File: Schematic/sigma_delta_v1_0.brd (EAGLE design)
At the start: 160 x 100 mm, 53 parts, among them IC2 MC78M12CDTG, IC3 UA78M33DCY, J1 SJ1-3523N, Q1 BS170, Q2 BS170, Q3 IRF3707S, Q4 IRF3707S, Q5 BSD223P, X1 1751251, X2 1751248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

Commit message: continued replaceing parts with smd components
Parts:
- removed Q1, Q2: BS170, transistor-small-signal:SOT54E
- added SJ1: (no value), jumper:SJ_2
- added U$4: BSD235N, SamacSys_Parts:SOT65P210X100-6N
- C1: device eagle-ltspice:C3640 -> rcl:C2220K
- C10, C9: device rcl:E2,5-7 -> rcl:UD-10X10_NICHICON
- C2, C3: device rcl:E2-5 -> rcl:UD-6,3X7,7_NICHICON
- moved D2 169.4 mm to (101.6, 31.8), turned to 270 degrees
- moved R8 139.9 mm to (92.7, 36.8), turned to 180 degrees
- moved R14 139.5 mm to (74.9, 44.5), turned to 90 degrees
- moved R13 133.6 mm to (74.9, 49.5), turned to 270 degrees
- moved R7 133.3 mm to (94.0, 57.1), turned to 180 degrees
- moved R15 130.8 mm to (61.0, 44.5), turned to 270 degrees
- moved D3 122.5 mm to (101.6, 52.1), turned to 270 degrees
- moved C7 121.9 mm to (45.7, 76.2), turned to 90 degrees
- moved C3 113.3 mm to (45.7, 69.8), turned to 90 degrees
- moved C6 106.7 mm to (34.3, 76.2), turned to 90 degrees
- moved C12 95.3 mm to (31.8, 76.2), turned to 90 degrees
- moved R4 94.6 mm to (64.8, 50.8), turned to 270 degrees
- moved C2 93.0 mm to (34.3, 69.8), turned to 90 degrees
- moved C11 88.9 mm to (20.3, 73.7), turned to 270 degrees
- moved R12 87.6 mm to (27.9, 26.7), turned to 270 degrees
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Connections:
- removed net VCC: J1.1
- new net N$27: C11.1, IC2.1, SJ1.2
- net GND: now also U$4.1, U$4.4; no longer Q1.S, Q2.S
- net N$11: now also U$4.5; no longer Q2.G
- net N$12: now also U$4.2; no longer Q1.G
- net N$3: now also U$4.6; no longer Q1.D
- net N$4: now also U$4.3; no longer Q2.D
- net VCC_HI: now also SJ1.3; no longer C11.1, IC2.1
- net VCC_MID: now also J1.1, SJ1.1
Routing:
- added copper zone on layer 1, net GND

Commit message: finished rework of the Schematic and cleaned up repository
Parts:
- removed JP2: (no value), pinhead:1X04SMD
- removed OK1, OK2: 6N137, optocoupler:DIL08
- removed X3: 1751264, con-phoenix-350:1751264
- added C13, C14: (no value), rcl:C0603
- added C8: 100n, rcl:C0603
- added IC1, IC4: LM50, linear:SOT23
- added IC5: ACPL-064L-000E, SamacSys_Parts:SOIC127P599X330-8N
- added JP1: (no value), pinhead:2X03
- added R17, R18: 10, eagle-ltspice:R0603
- added X4: 1751280, con-phoenix-350:1751280
- C11, C6: value (none) -> 330n
- C12, C7: value (none) -> 100n
- R1, R2: value 270 -> 1k
- moved R16 14.5 mm to (53.3, 45.7), turned to 180 degrees
- moved R15 8.52 mm to (53.3, 48.3), turned to 180 degrees
- moved Q5 5.08 mm to (64.8, 47.0)
- moved R3 4.02 mm to (57.1, 49.5)
- turned R4 to 180 degrees
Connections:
- net N$26 renamed H_BRIDGE_MID
- new net N$26: IC5.7, R15.2
- new net N$28: C13.1, JP1.1, R17.1, X4.1
- new net N$29: C14.1, JP1.5, R18.1, X4.5
- new net N$32: IC1.2, R18.2
- net GND: now also C13.2, C14.2, C8.2, IC1.3, IC4.3, IC5.5, JP1.6, X4.6; no longer JP2.1, OK1.5, OK2.5, X3.1
- net N$1: now also JP1.3, X4.3; no longer JP2.4, X3.4
- net N$2: now also JP1.4, X4.4; no longer JP2.3, X3.3
- net N$23: now also IC4.2, R17.2; no longer OK2.6, R16.2
- net N$3: now also IC5.2; no longer OK1.3
- net N$4: now also IC5.3; no longer OK2.3
- net N$5: now also IC5.1; no longer OK1.2
- net N$6: now also IC5.4; no longer OK2.2
- net N$8: now also IC5.6, R16.2; no longer OK1.6, R15.2
- net VCC_3.3: now also C8.1, IC1.1, IC4.1, IC5.8; no longer OK1.7, OK1.8, OK2.7, OK2.8
- net VCC_FPGA: now also JP1.2, X4.2; no longer JP2.2, X3.2

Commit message: started layout design
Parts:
- moved C14 61.1 mm to (24.1, 40.6), flipped to the bottom
- moved R18 57.9 mm to (27.9, 40.6), flipped to the bottom
- moved R17 55.7 mm to (27.9, 43.2), flipped to the bottom
- moved C13 50.6 mm to (24.1, 43.2), flipped to the bottom
- moved IC2 18.2 mm to (29.2, 62.2)
- moved C10 18.2 mm to (27.9, 34.3)
- moved C12 18.2 mm to (35.6, 58.4)
- moved C6 18.2 mm to (38.1, 58.4)
- moved C7 18.2 mm to (49.5, 58.4)
- moved C11 18.2 mm to (24.1, 55.9)
- moved C2 18.2 mm to (38.1, 52.1)
- moved C3 18.2 mm to (49.5, 52.1)
- moved C9 18.2 mm to (27.9, 47.0)
- moved IC3 18.2 mm to (43.2, 61.0)
- moved SJ1 13.6 mm to (20.3, 60.3)
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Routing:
- net VCC_MID: track 0.00 -> 29.9 mm
- net VCC_HI: track 0.00 -> 23.2 mm, vias 48 -> 50
- net VCC_FPGA: track 0.00 -> 21.3 mm
- net VCC_12: track 0.00 -> 13.0 mm
- net N$2: track 0.00 -> 12.9 mm
- net N$1: track 0.00 -> 12.8 mm
- net N$27: track 0.00 -> 9.79 mm
- net N$9: track 0.00 -> 7.90 mm
- net N$18: track 0.00 -> 7.90 mm
- net N$20: track 0.00 -> 7.59 mm
- net VCC_3.3: track 0.00 -> 7.48 mm
- added copper zone on layer 16, net GND

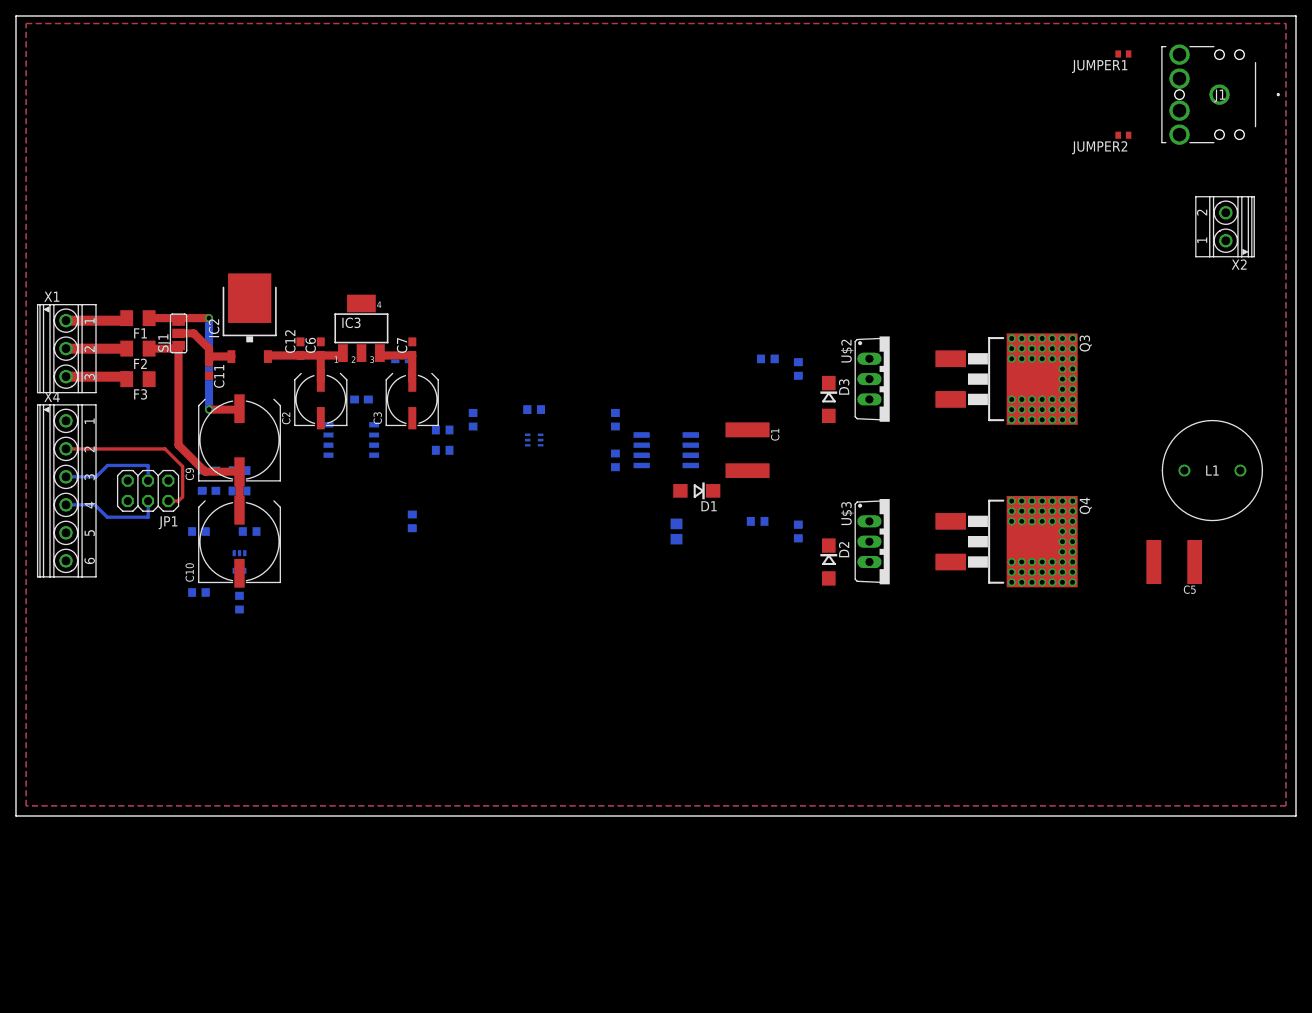
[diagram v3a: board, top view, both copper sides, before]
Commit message: continued layouting and added analog decoupling for temperature sensors
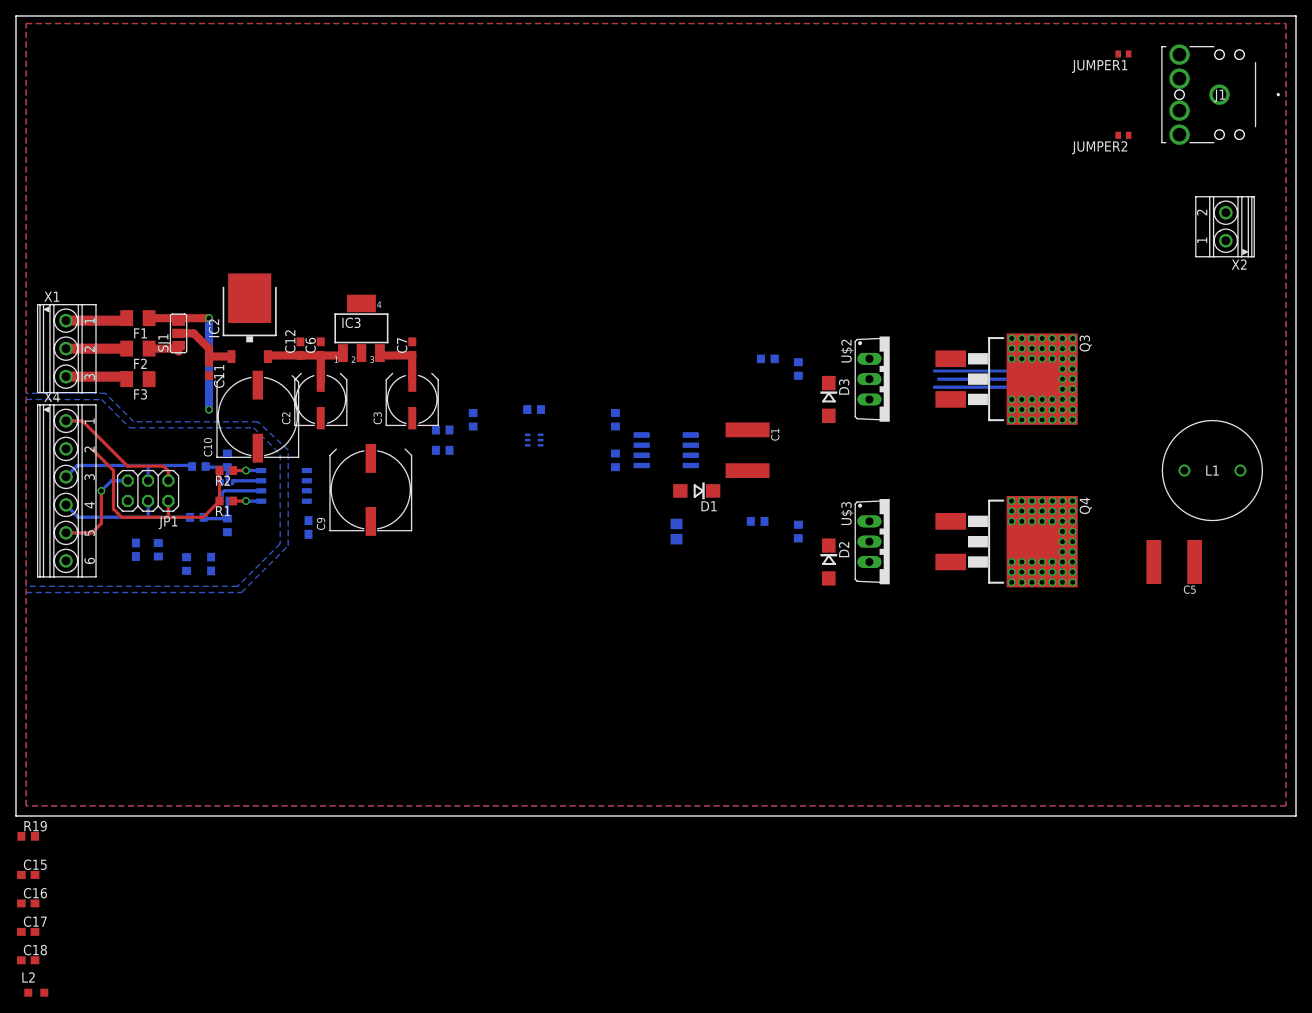
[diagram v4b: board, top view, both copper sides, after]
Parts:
- added C15, C17: 0.1µ, rcl:C0603
- added C16, C18: 1µ, rcl:C0603
- added L2: TBD, rcl:L2012C
- added R19: 50, eagle-ltspice:R0603
- moved R2 26.0 mm to (26.3, 43.2), flipped to the top, turned to 180 degrees
- moved R1 23.4 mm to (26.3, 39.4), flipped to the top, turned to 180 degrees
- moved R12 17.8 mm to (26.4, 44.5), turned to 90 degrees
- moved C9 17.5 mm to (44.3, 40.8)
- moved C8 17.3 mm to (36.6, 36.1), turned to 270 degrees
- moved C10 15.8 mm to (30.2, 49.9)
- moved R6 15.7 mm to (22.9, 43.7), turned to 0 degrees
- moved R17 13.4 mm to (21.3, 31.5), turned to 270 degrees
- moved R18 12.5 mm to (17.8, 33.3), turned to 270 degrees
- moved C14 11.7 mm to (15.0, 33.3), turned to 270 degrees
- moved C13 11.7 mm to (24.4, 31.5), turned to 270 degrees
- moved IC5 10.2 mm to (33.5, 41.3), turned to 180 degrees
- moved U$4 9.02 mm to (26.4, 40.6), turned to 270 degrees
- moved R11 2.90 mm to (26.4, 36.3), turned to 270 degrees
- moved R5 1.80 mm to (22.6, 37.3), turned to 0 degrees
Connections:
- new net AGND_FPGA: C13.2, C14.2, C15.2, C16.2, IC1.3, IC4.3, L2.2
- new net AVCC_FPGA: C15.1, C16.1, IC1.1, IC4.1, R19.1
- new net GND_FPGA: JP1.6, R11.2, R12.2, U$4.1, U$4.4, X4.6
- net GND: now also C17.2, C18.2, L2.1; no longer C13.2, C14.2, IC1.3, IC4.3, JP1.6, R11.2, R12.2, U$4.1, U$4.4, X4.6
- net VCC_3.3: no longer IC1.1, IC4.1
- net VCC_FPGA: now also C17.1, C18.1, R19.2
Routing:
- net VCC_MID: track 29.9 -> 4.38 mm
- net N$28: track 0.00 -> 16.6 mm
- net N$29: track 0.00 -> 12.8 mm, vias 0 -> 1
- net AGND_FPGA: track 0.00 -> 12.8 mm
- net N$23: track 0.00 -> 11.1 mm
- net AVCC_FPGA: track 0.00 -> 11.1 mm
- net VCC_FPGA: track 21.3 -> 29.0 mm
- net N$3: track 0.00 -> 5.83 mm
- net N$1: track 12.8 -> 18.3 mm
- net N$11: track 0.00 -> 5.40 mm
- net N$2: track 12.9 -> 18.2 mm
- net N$12: track 0.00 -> 4.60 mm
- net VCC_HI: track 23.2 -> 19.3 mm
- net N$4: track 0.00 -> 3.70 mm
- net N$6: track 0.00 -> 3.51 mm, vias 0 -> 1
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- added copper zone on layer 16, net GND_FPGA

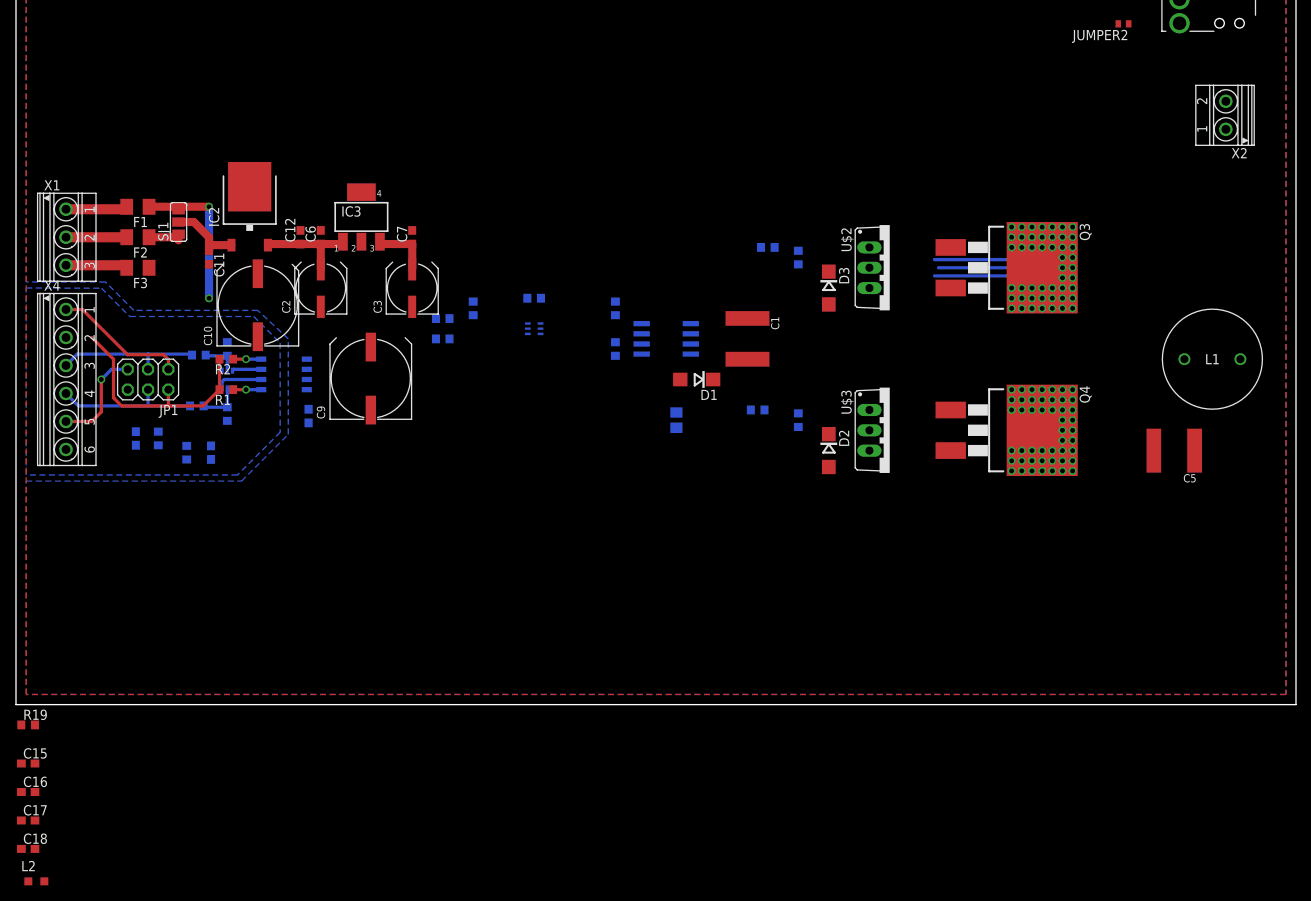
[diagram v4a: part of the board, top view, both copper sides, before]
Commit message: continued routing and added ferrit bead datasheet
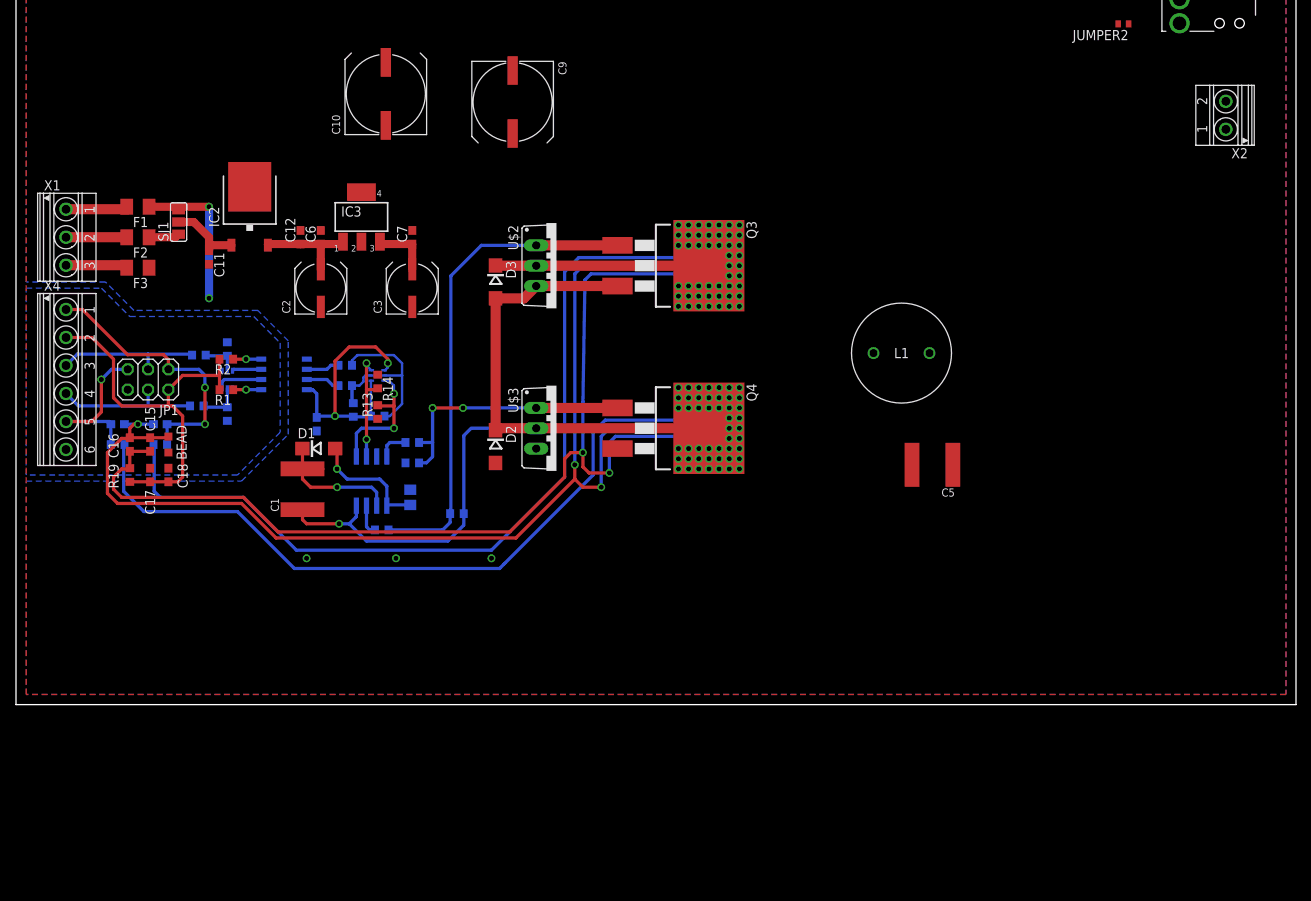
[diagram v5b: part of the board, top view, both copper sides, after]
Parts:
- removed L2: TBD, rcl:L2012C
- added BEAD: MMZ0603S102HT000, rcl:L2012C
- moved R7 59.8 mm to (45.7, 21.8), turned to 0 degrees
- moved C1 58.7 mm to (35.8, 26.9), turned to 90 degrees
- moved R9 53.3 mm to (55.1, 23.9), turned to 180 degrees
- moved C18 49.9 mm to (19.1, 28.7), turned to 90 degrees
- moved R10 48.6 mm to (49.5, 30.2), turned to 0 degrees
- moved D1 48.0 mm to (37.8, 32.0), turned to 0 degrees
- moved C17 45.8 mm to (16.8, 28.7), turned to 90 degrees
- moved C16 45.3 mm to (14.2, 32.5), turned to 90 degrees
- moved R8 43.4 mm to (49.5, 32.8), turned to 0 degrees
- moved C15 42.7 mm to (16.8, 32.5), turned to 90 degrees
- moved D3 41.7 mm to (59.9, 52.8)
- moved D2 41.7 mm to (59.9, 32.3)
- moved IC1 41.7 mm to (85.3, 34.5)
- moved IC4 41.7 mm to (85.3, 54.9)
- moved Q3 41.7 mm to (84.1, 54.9)
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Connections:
- net AGND_FPGA: now also BEAD.2; no longer L2.2
- net GND: now also BEAD.1; no longer L2.1
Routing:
- net AGND_FPGA: track 12.8 -> 149.8 mm, vias 0 -> 3
- net AVCC_FPGA: track 11.1 -> 129.7 mm, vias 0 -> 2
- net H_BRIDGE_MID: track 0.00 -> 105.7 mm, vias 48 -> 49
- net N$23: track 11.1 -> 106.1 mm
- net N$32: track 0.00 -> 91.5 mm
- net N$14: track 0.00 -> 61.3 mm
- net N$15: track 0.00 -> 32.9 mm, vias 0 -> 2
- net VCC_3.3: track 7.48 -> 40.0 mm, vias 0 -> 2
- net VCC_HI: track 19.3 -> 46.0 mm
- net VCC_FPGA: track 29.0 -> 48.9 mm
- net N$28: track 16.6 -> 34.9 mm, vias 0 -> 2
- net N$17: track 0.00 -> 18.0 mm, vias 0 -> 1
- net N$22: track 0.00 -> 17.7 mm
- net N$19: track 0.00 -> 16.7 mm, vias 0 -> 2
- net VCC_12: track 13.0 -> 28.1 mm, vias 0 -> 1
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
